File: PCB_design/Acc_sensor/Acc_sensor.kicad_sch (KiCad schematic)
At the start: 37 parts, among them Q1 NMOS, Q2 NMOS, SW1 SW_SPST, U1 ESP32-C3, U2 LIS2DE12, U3 DW01A, U3 MAX17263xxTE, U4 MAX30102, U5 TPS22917LDBV, U7 TLV75533PDBV

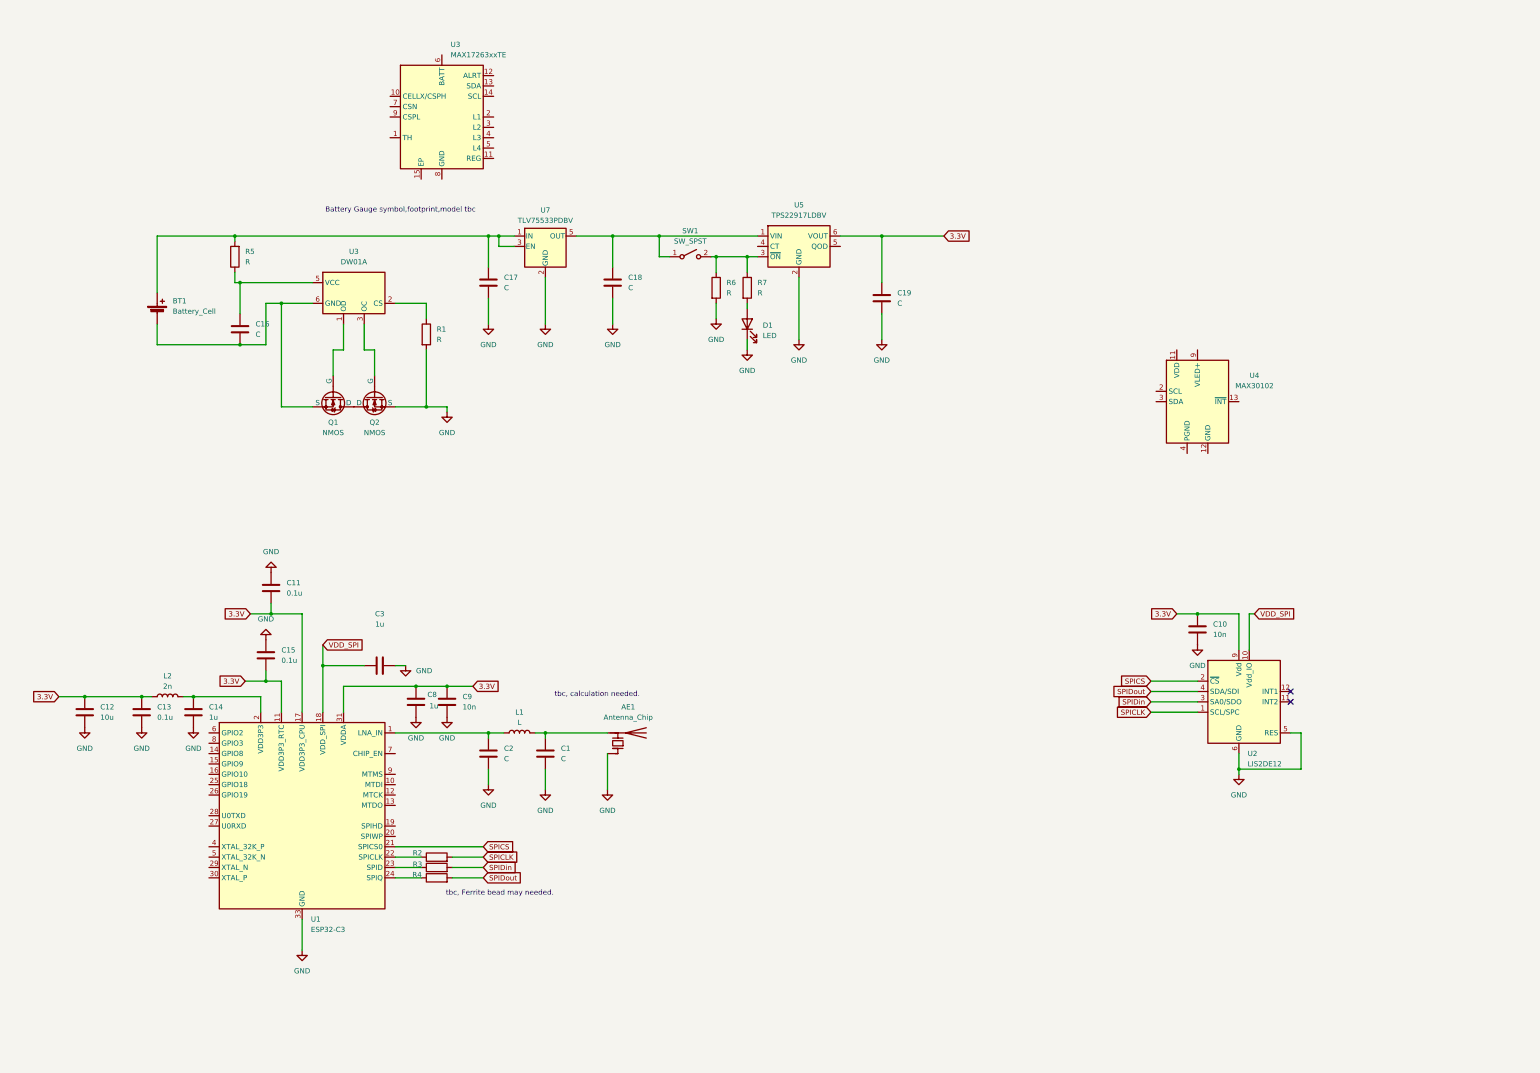
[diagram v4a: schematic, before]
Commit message: modify
chipenable, I2C pullup, RC value comfirmed.
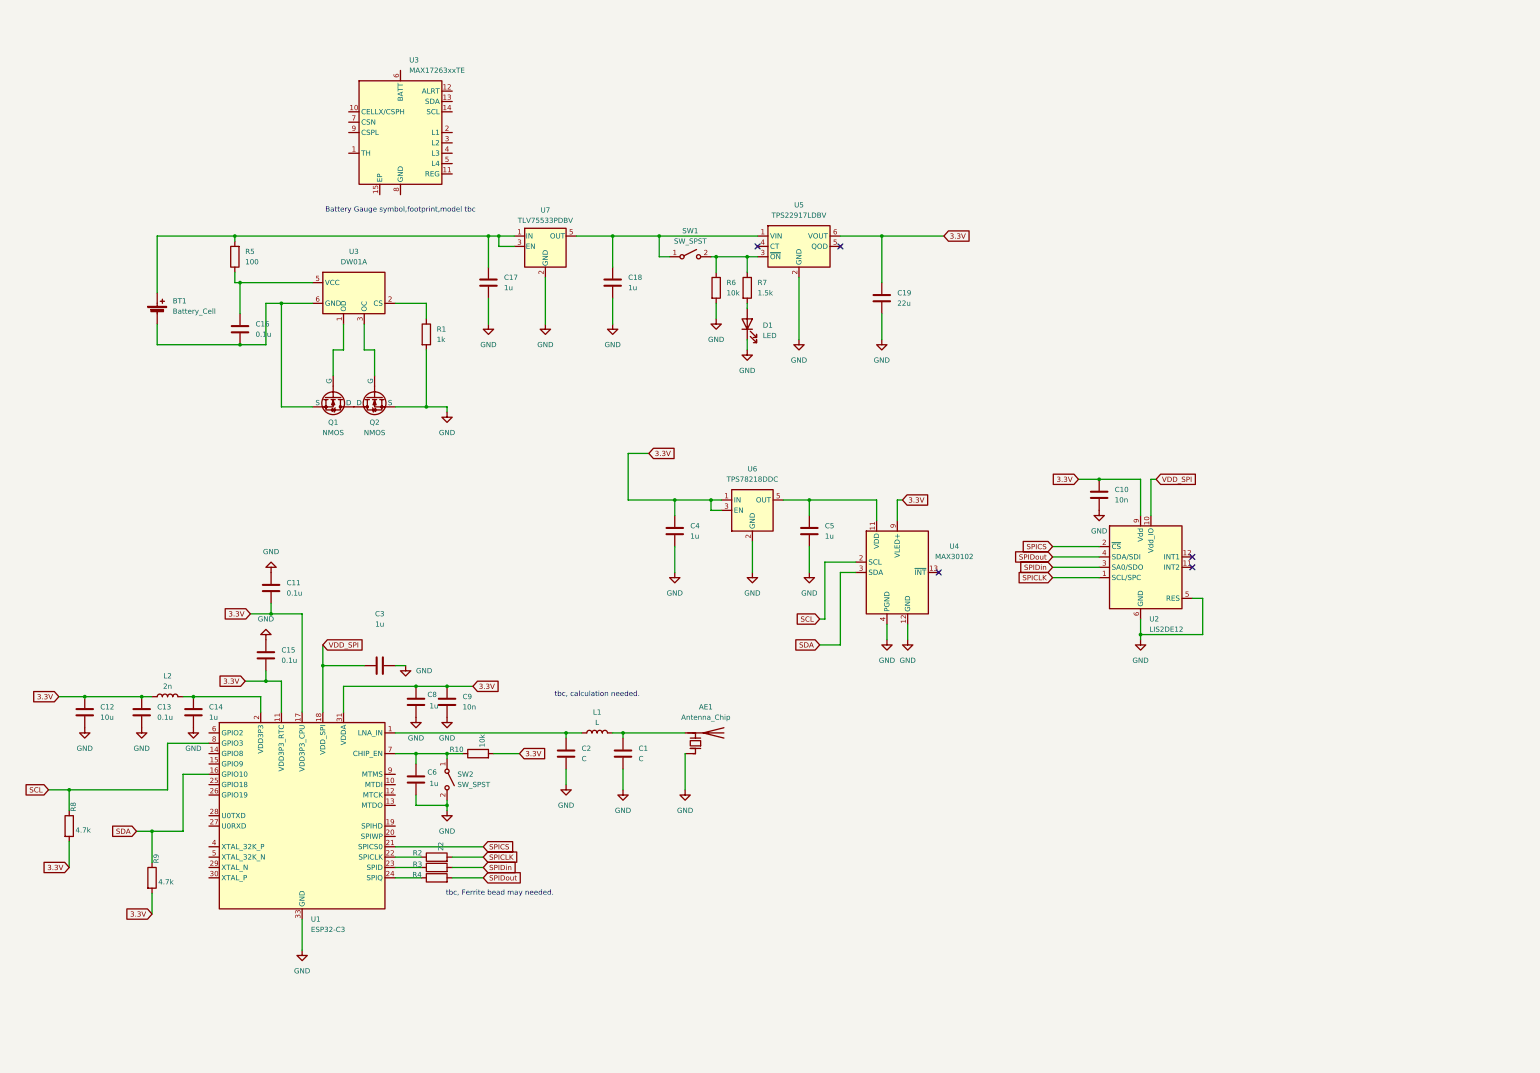
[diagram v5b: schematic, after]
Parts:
- added C4, C5, C6: 1u, symbol Device:C
- added R10: 10k, symbol Device:R
- added R8, R9: 4.7k, symbol Device:R
- added SW2: SW_SPST, symbol Switch:SW_SPST
- added U6: TPS78218DDC, Package_TO_SOT_SMD:SOT-23-5, symbol Regulator_Linear:TPS78218DDC
- C16: value C -> 0.1u
- C17, C18: value C -> 1u
- C19: value C -> 22u
- R1: value R -> 1k
- R5: value R -> 100
- R6: value R -> 10k
- R7: value R -> 1.5k
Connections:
- net 3.3V: now also U4.10 (VLED+), U4.9 (VLED+), C4.1, R10.2, R8.2, R9.2, U6.1 (IN), U6.3 (EN)
- net GND: now also U4.12 (GND), U4.4 (PGND), C4.2, C5.2, C6.2, SW2.2 (B), U6.2 (GND), U6.4 (GND)
- net SDA: now reaches U1.16 (GPIO10)
- net SDA: now also U4.3 (SDA), R9.1
- net at U1.7 (CHIP_EN): now also C6.1, R10.1, SW2.1 (A)
- net SCL: now reaches U1.8 (GPIO3)
- net SCL: now also U4.2 (SCL), R8.1
- net at U4.11 (VDD): now also C5.1, U6.5 (OUT)
- no-connect marks 2 -> 5
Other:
- moved on the sheet: AE1, C1, C10, C2, L1, U2, U3, U4

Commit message: usb
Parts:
- added C20, C7: 20p, symbol Device:C
- added C21: 1u, symbol Device:C
- added C22: 0805_10n, symbol Device:C
- added D2: LED, symbol Device:LED
- added J1: Conn_01x04_Socket, symbol Connector:Conn_01x04_Socket
- added J2: Conn_01x04_Pin, symbol Connector:Conn_01x04_Pin
- added J3: USB_C_Receptacle_USB2.0_16P, symbol Connector:USB_C_Receptacle_USB2.0_16P
- added R11: 0, symbol Device:R
- added R12, R13, R14: 10k, symbol Device:R
- added R15, R16: 0805_5k1, symbol Device:R
- added R17: 0805_1M, symbol Device:R
- added R18: 4.7k, symbol Device:R
- added R19, R20: 100k, symbol Device:R
- added SW3: SW_SPST, symbol Switch:SW_SPST
- added Y1: Crystal_GND24, symbol Device:Crystal_GND24
- C1: value C -> 1.8-1.2p
- C2: value C -> 1.2-1.8p
- L1: value L -> 2.4-3.0n
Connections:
- net 3.3V: now also R8.1, R9.1, J1.1 (Pin_1), J2.1 (Pin_1), R12.2, R13.1, R14.1; no longer R8.2, R9.2
- net GND: now also C20.1, C21.2, C22.1, C7.2, D2.1 (K), J1.4 (Pin_4), J2.4 (Pin_4), J3.A1 (GND), J3.A12 (GND), J3.B1 (GND), J3.B12 (GND), R15.1, R16.1, R17.2, SW3.2 (B), Y1.2, Y1.4
- net SCL: now also R8.2; no longer R8.1
- net SDA: now also R9.2; no longer R9.1
- net at U1.14 (GPIO8): now also R14.2
- net at U1.15 (GPIO9): now also C21.1, R12.1, SW3.1 (A)
- net at U1.25 (GPIO18): now also J1.2 (Pin_2)
- net at U1.26 (GPIO19): now also J1.3 (Pin_3)
- net at U1.29 (XTAL_N): now also R11.2
- net at U1.30 (XTAL_P): now also C7.1, Y1.3
- net at U1.4 (XTAL_32K_P): now also R18.2
- net at U1.5 (XTAL_32K_N): now also R19.2, R20.2
- net at U1.6 (GPIO2): now also R13.2
- new net: C20.2, R11.1, Y1.1
- new net: C22.2, J3.S1 (SHIELD), R17.1
- new net: D2.2 (A), R18.1
- new net: J3.B5 (CC2), R16.2
- new net: J3.A5 (CC1), R15.2
- new net USB N: J2.2 (Pin_2), J3.A7 (D-), J3.B7 (D-)
- new net USB P: J2.3 (Pin_3), J3.A6 (D+), J3.B6 (D+)
- new net Vbus: J3.A4 (VBUS), J3.A9 (VBUS), J3.B4 (VBUS), J3.B9 (VBUS), R19.1
- no-connect marks 5 -> 7
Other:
- note added: "USB LED"
- note added: "Vbat"
- note added: "footprint smaller, better"
- moved on the sheet: AE1, BT1, C1, C10, C11, C12, C13, C14, C15, C16, C17, C18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
